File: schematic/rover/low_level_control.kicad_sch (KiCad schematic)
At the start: 0 parts

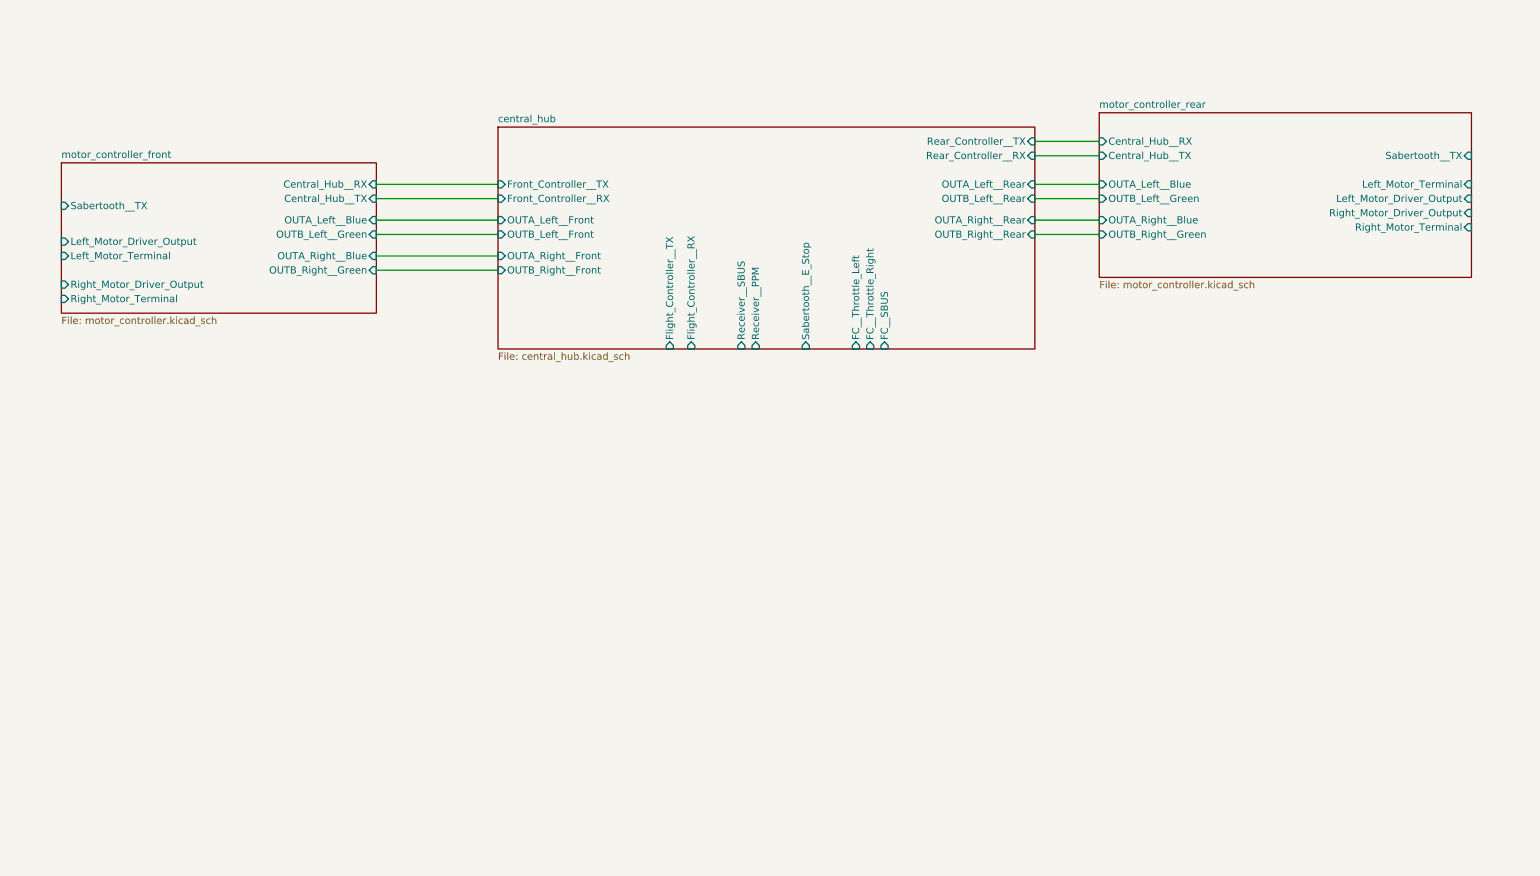
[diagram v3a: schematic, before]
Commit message: Complete power board and motor wiring
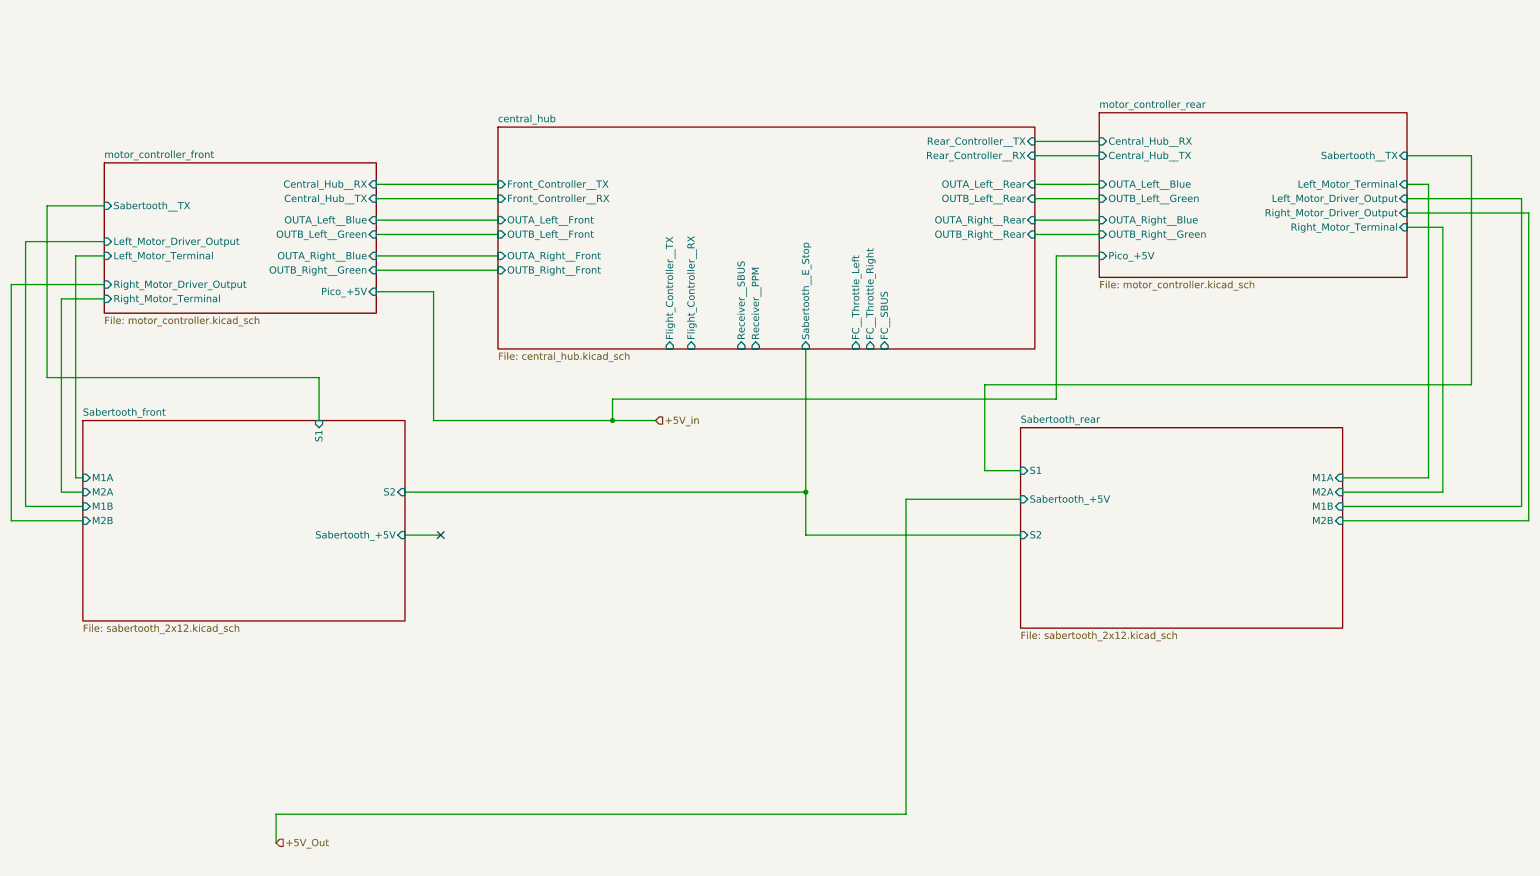
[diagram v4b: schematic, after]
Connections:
- no-connect marks 0 -> 1
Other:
- added sheet Sabertooth_front (sabertooth_2x12.kicad_sch)
- added sheet Sabertooth_rear (sabertooth_2x12.kicad_sch)
- sheet motor_controller_front ports: added Pico_+5V; removed none
- sheet motor_controller_rear ports: added Pico_+5V; removed none
